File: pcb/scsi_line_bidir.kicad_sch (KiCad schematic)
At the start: 0 parts

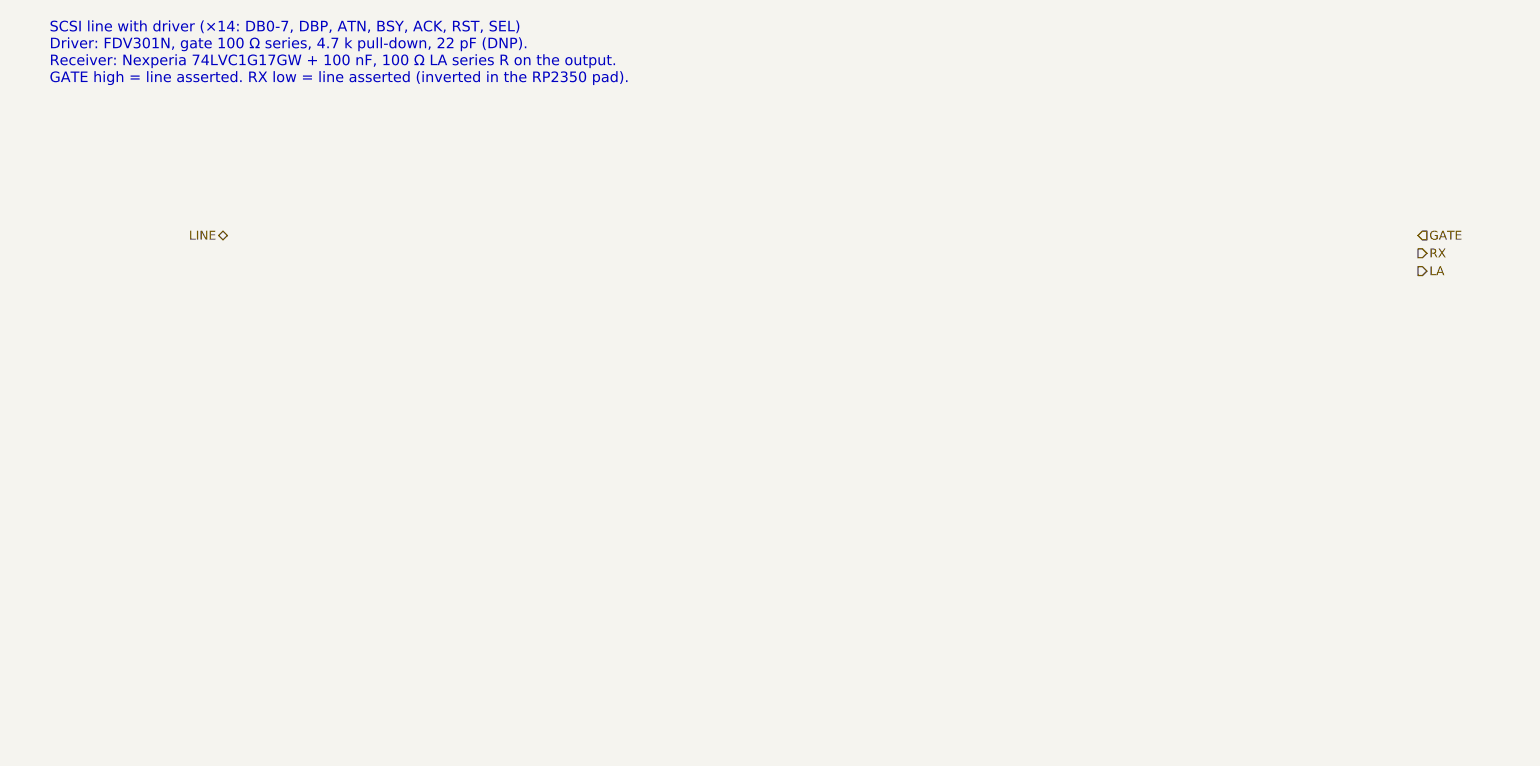
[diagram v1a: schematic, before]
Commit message: Phase 3: populate SCSI sheet and channel sheets
SCSI sheet (A2): IDC50 and HD50 wired by signal name from SCSI-2
Table 2, all four RESERVED lines grounded through 0R links, the
logic-analyzer header as a pin-for-pin copy of the Digital Discovery
DIN connector, three SN74LVTH245A terminators with their DIP-switch
enable and truth table, and one cluster per line: 2 x 220R terminator
pair, ESD diode and channel sheet. Channel sheets hold the FDV301N
driver and the 74LVC1G17 receiver; 18 instances, references page x 100.

Generator: repeated sheets, sheet symbols, native tables, and
deterministic UUIDs. Nets renamed: LA -> LOGIC_ANALYZER,
TERMINATOR_EN -> TERMINATOR_EN_INVERTED_FIRMWARE.
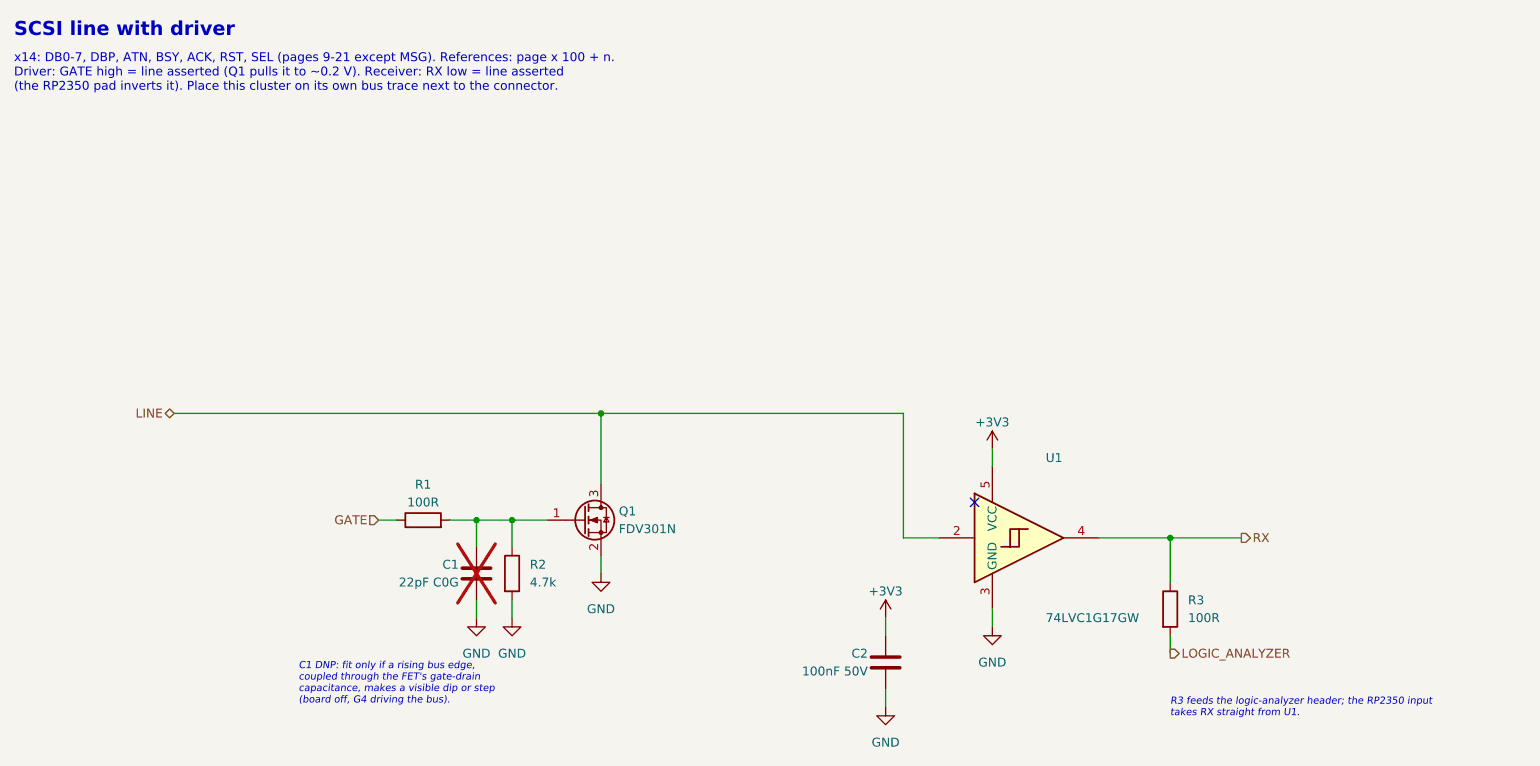
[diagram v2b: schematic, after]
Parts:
- added C1: 22pF C0G, Capacitor_SMD:C_0402_1005Metric, symbol Device:C
- added C2: 100nF 50V, Capacitor_SMD:C_0402_1005Metric, symbol Device:C
- added Q1: FDV301N, Package_TO_SOT_SMD:SOT-23, symbol Transistor_FET:Q_NMOS_GSD
- added R1, R3: 100R, Resistor_SMD:R_0402_1005Metric, symbol Device:R
- added R2: 4.7k, Resistor_SMD:R_0402_1005Metric, symbol Device:R
- added U1: 74LVC1G17GW, Package_TO_SOT_SMD:SOT-353_SC-70-5, symbol 74xGxx:74LVC1G17
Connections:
- net GATE: now also R1.1
- net LINE: now also Q1.3 (D), U1.2
- net RX: now also R3.1, U1.4
- new net: C1.1, Q1.1 (G), R1.2, R2.1
- new net +3V3: C2.1, U1.5 (VCC)
- new net GND: C1.2, C2.2, Q1.2 (S), R2.2, U1.3 (GND)
- new net LOGIC_ANALYZER: R3.2
- no-connect marks 0 -> 1
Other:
- note added: "C1 DNP: fit only if a rising bus edge, coupled through the FET's gate-drain capacitance, makes a visible dip or step (board off, G4 driving the bus)."
- note added: "R3 feeds the logic-analyzer header; the RP2350 input takes RX straight from U1."
- note added: "SCSI line with driver"
- note added: "x14: DB0-7, DBP, ATN, BSY, ACK, RST, SEL (pages 9-21 except MSG). References: page x 100 + n. Driver: GATE high = line asserted (Q1 pulls it to ~0.2 V). Receiver: RX low = line asserted (the RP2350 pad inverts it). Place this cluster on its own bus trace next to the connector."
- note removed: "SCSI line with driver (×14: DB0-7, DBP, ATN, BSY, ACK, RST, SEL) Driver: FDV301N, gate 100 Ω series, 4.7 k pull-down, 22 pF (DNP). Receiver: Nexperia 74LVC1G17GW + 100 nF, 100 Ω LA series R on the output. GATE high = line asserted. RX low = line asserted (inverted in the RP2350 pad)."

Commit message: route more scsi traces
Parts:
- renumbered C1 to C901, C2 to C902, Q1 to Q901, R1 to R901, R2 to R902, R3 to R903, U1 to U901
